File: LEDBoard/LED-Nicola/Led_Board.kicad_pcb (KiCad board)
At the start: 2 copper layers, 107.9 x 67.3 mm, 34 parts, among them J1 MOUNTING_HOLE, J10 CONN_01X02, J11 LED CONN 01X16, J12 CONN_01X02, J13 LED CONN 01X04, J2 MOUNTING_HOLE, J3 MOUNTING_HOLE, J4 MOUNTING_HOLE, J5 Arduino CONN 01X04, J6 Arduino CONN_01X04, J7 Arduino CONN_01X06, J8 VD 0 CONN_01X02, J9 CONN_01X02, Q1 MMBT, U1 SSR

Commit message: Changes
plz let me push
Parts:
- added BZ101: Buzzer, hyperCustom:nicolaBuzzer, F.Cu at (101.0, 81.9)
- added R101: R, Resistors_ThroughHole:R_Axial_DIN0309_L9.0mm_D3.2mm_P12.70mm_Horizontal, F.Cu at (178.4, 111.1)
- added R102: R, Resistors_ThroughHole:R_Axial_DIN0309_L9.0mm_D3.2mm_P12.70mm_Horizontal, F.Cu at (89.5, 95.9)
- Q1: value MMBT -> MMBT2222ALT1G
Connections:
- net /GND renamed GND
- U1 pad 5: /Buzzer -> Net-(R101-Pad2)
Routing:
- net /5V0: track 19.9 -> 72.9 mm, vias 0 -> 1
- net Net-(BZ101-Pad1): track 0.00 -> 15.1 mm
- net Net-(R101-Pad2): track 0.00 -> 12.1 mm
- added copper zone on B.Cu, net /GND

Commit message: new changes
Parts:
- removed BZ101: Buzzer, hyperCustom:nicolaBuzzer
- removed R101, R102: R, Resistors_ThroughHole:R_Axial_DIN0309_L9.0mm_D3.2mm_P12.70mm_Horizontal
- Q1: value MMBT2222ALT1G -> MMBT
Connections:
- D1 pad 1: GND -> /GND
- J1 pad 1: GND -> /GND
- J11 pad 10: GND -> /GND
- J11 pad 12: GND -> /GND
- J11 pad 14: GND -> /GND
- J11 pad 16: GND -> /GND
- J11 pad 2: GND -> /GND
- J11 pad 4: GND -> /GND
- J11 pad 6: GND -> /GND
- J11 pad 8: GND -> /GND
- J12 pad 2: GND -> /GND
- J13 pad 2: GND -> /GND
- J13 pad 4: GND -> /GND
- J2 pad 1: GND -> /GND
- J3 pad 1: GND -> /GND
- J4 pad 1: GND -> /GND
- J7 pad 2: GND -> /GND
- Q1 pad 2: GND -> /GND
- R11 pad 2: GND -> /GND
- R13 pad 2: GND -> /GND
- R9 pad 2: GND -> /GND
- U1 pad 5: Net-(R101-Pad2) -> /Buzzer
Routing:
- net /5V0: track 72.9 -> 19.9 mm, vias 1 -> 0
- net Net-(BZ101-Pad1): track 15.1 -> 0.00 mm
- net Net-(R101-Pad2): track 12.1 -> 0.00 mm
- net GND: track 2.06 -> 0.00 mm, vias 17 -> 0
- net /GND: track 0.00 -> 2.06 mm, vias 0 -> 17
- removed copper zone on B.Cu, net GND

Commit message: changes
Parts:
- removed G***: LOGO, hyperCustom:ParadigmLogo_1x1
- added BZ101: , hyperCustom:nicolaBuzzer, F.Cu at (101.0, 81.9)
- added R101: , Resistors_ThroughHole:R_Axial_DIN0309_L9.0mm_D3.2mm_P12.70mm_Horizontal, F.Cu at (178.4, 111.1)
- added R102: , Resistors_ThroughHole:R_Axial_DIN0309_L9.0mm_D3.2mm_P12.70mm_Horizontal, F.Cu at (89.5, 95.9)
- D1: value LED -> (none)
- J1, J2, J3, J4: value MOUNTING_HOLE -> (none)
- J10, J12, J9: value CONN_01X02 -> (none)
- J11: value LED CONN 01X16 -> (none)
- J13: value LED CONN 01X04 -> (none)
- J5: value Arduino CONN 01X04 -> (none)
- J6: value Arduino CONN_01X04 -> (none)
- J7: value Arduino CONN_01X06 -> (none)
- J8: value VD 0 CONN_01X02 -> (none)
- R1, R15, R16, R17, R2, R3, R4, R5, R6, R7: value 220 -> (none)
- R10, R11, R12, R13, R14, R8, R9: value R -> (none)
- moved D1 19.4 mm to (166.4, 80.0), turned to 270 degrees
- moved R13 12.5 mm to (175.3, 88.9), turned to 270 degrees
- moved R14 11.7 mm to (170.2, 80.0), turned to 270 degrees
- moved R12 9.25 mm to (179.1, 88.9)
- moved J8 9.00 mm to (193.0, 83.8)
- moved R8 8.98 mm to (177.8, 80.0)
- moved J10 8.78 mm to (193.0, 92.7)
- moved R9 7.41 mm to (174.0, 80.0), turned to 270 degrees
- moved R11 5.24 mm to (175.3, 69.8), turned to 270 degrees
- moved R10 4.02 mm to (180.3, 69.8)
- moved U1 1.27 mm to (167.6, 101.6), turned to 90 degrees
- moved J9 0.11 mm to (193.0, 74.9)
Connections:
- J5 pad 1: /A1 -> /A0
- J5 pad 2: /A0 -> /24V
- J5 pad 3: /24V -> /5V0
- J5 pad 4: /5V0 -> /Transistor
- J6 pad 1: /A5 -> /A4
- J6 pad 2: /A4 -> /A3
- J6 pad 3: /A3 -> /A2
- J6 pad 4: /A2 -> /A1
- J7 pad 1: (no net) -> /ArduinoLED
- J7 pad 2: /GND -> /5V
- J7 pad 3: /A9 -> /A8
- J7 pad 4: /A8 -> /A7
- J7 pad 5: /A7 -> /A6
- J7 pad 6: /A6 -> /A5
- Q1 pad 1: /A7 -> /Transistor
- R17 pad 2: /A9 -> /ArduinoLED
- U1 pad 5: /Buzzer -> Net-(R101-Pad2)
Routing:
- net /ArduinoLED: track 0.00 -> 46.5 mm
- net /A7: track 93.4 -> 49.0 mm, vias 1 -> 0
- net /A9: track 43.6 -> 0.00 mm
- net /24V: track 58.5 -> 39.3 mm, vias 2 -> 0
- net /VDO0: track 31.7 -> 14.9 mm
- net Net-(BZ101-Pad1): track 0.00 -> 15.1 mm
- net Net-(R101-Pad2): track 0.00 -> 15.0 mm, vias 0 -> 1
- net Net-(D1-Pad2): track 15.6 -> 4.02 mm
- net /5V: track 0.00 -> 11.0 mm, vias 0 -> 1
- net /Transistor: track 0.00 -> 6.69 mm
- net Net-(Q1-Pad3): track 7.87 -> 12.8 mm
- net /VDI1: track 8.73 -> 4.96 mm
- net /VDO2: track 13.1 -> 9.84 mm
- net /A0: track 58.8 -> 61.7 mm, vias 2 -> 0
- net /VDO1: track 13.1 -> 10.2 mm
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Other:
- board text added: "PWR IN"
- board text added: "PWR OUT"
- board text removed: "Nicola Duffy July 2017"
- board text removed: "PWR"

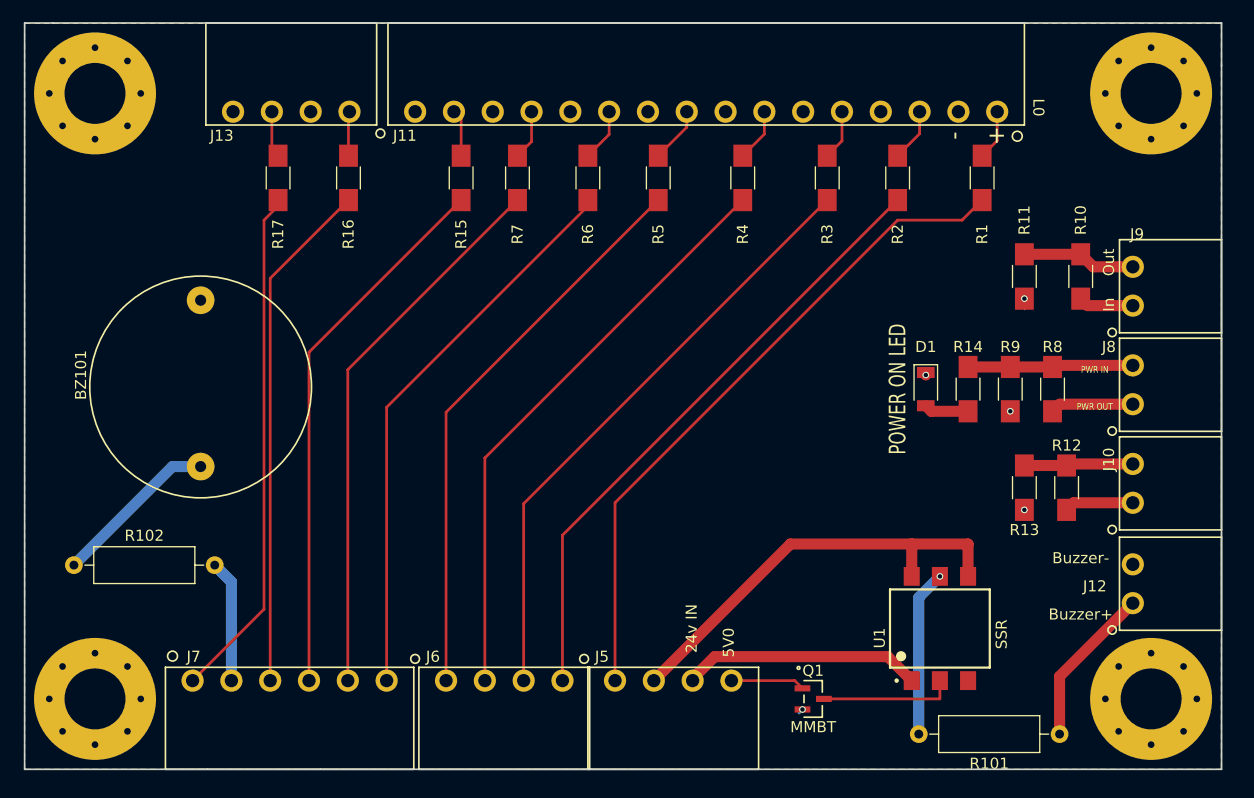
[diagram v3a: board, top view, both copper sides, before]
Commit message: Finalized LED Board
Added Silkscreen for all sides of the board and all connectors. Moved
the Placement of the Power on LED to show then the arduino is
outputting power correctly. Slightly move components to make it more
efficient.
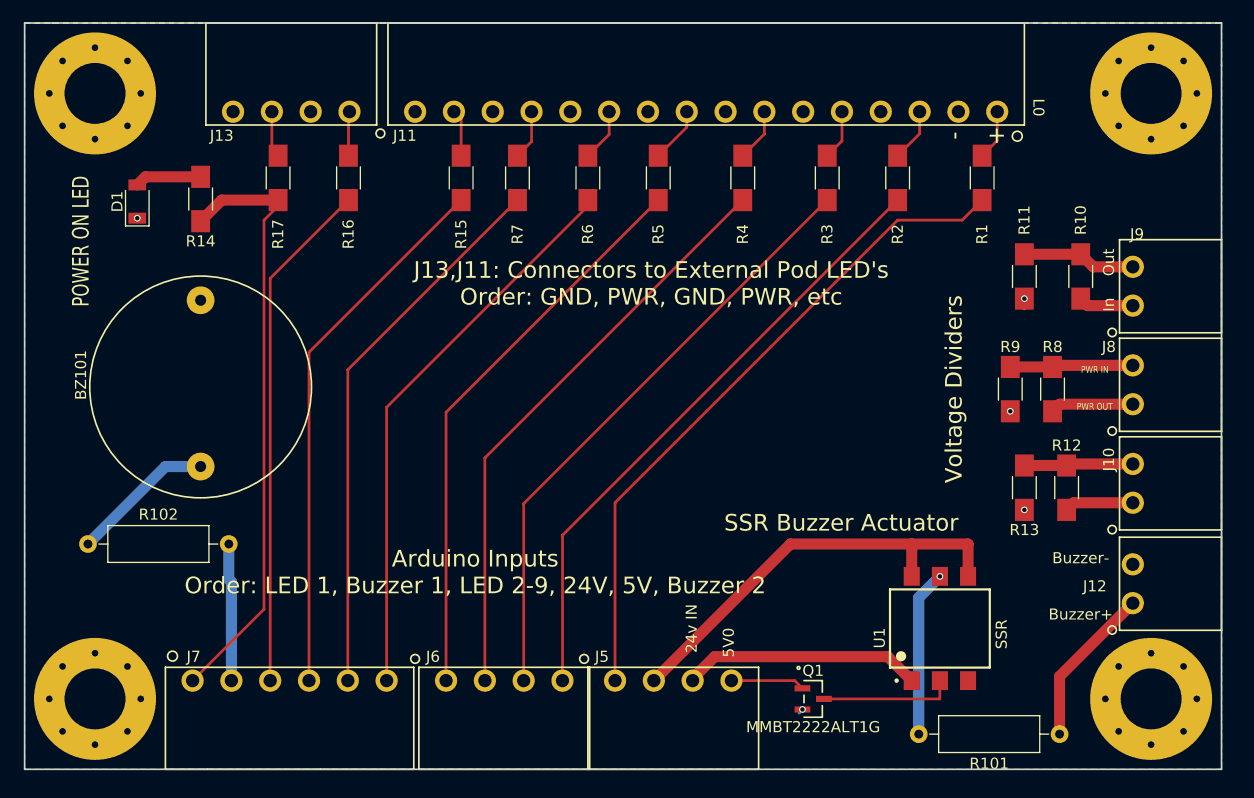
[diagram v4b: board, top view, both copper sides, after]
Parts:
- BZ101: value (none) -> Buzzer
- D1: value (none) -> LED
- J1, J2, J3, J4: value (none) -> MOUNTING_HOLE
- J10, J12, J9: value (none) -> CONN_01X02
- J11: value (none) -> LED CONN 01X16
- J13: value (none) -> LED CONN 01X04
- J5: value (none) -> Arduino CONN 01X04
- J6: value (none) -> Arduino CONN_01X04
- J7: value (none) -> Arduino CONN_01X06
- J8: value (none) -> VD 0 CONN_01X02
- Q1: value MMBT -> MMBT2222ALT1G
- R1, R15, R16, R17, R2, R3, R4, R5, R6, R7: value (none) -> 220
- R10, R101, R102, R11, R12, R13, R14, R8, R9: value (none) -> R
- moved D1 73.1 mm to (95.2, 63.1), turned to 90 degrees
- moved R14 71.3 mm to (101.0, 62.9), turned to 90 degrees
- moved R102 2.29 mm to (90.8, 94.0)
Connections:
- R14 pad 1: /VDO0 -> /ArduinoLED
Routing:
- net /ArduinoLED: track 46.5 -> 54.3 mm
- net /VDO0: track 14.9 -> 11.1 mm
- net Net-(BZ101-Pad1): track 15.1 -> 13.1 mm
- net Net-(D1-Pad2): track 4.02 -> 6.02 mm
- net /5V: track 11.0 -> 12.4 mm
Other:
- board text added: "Arduino Inputs Order: LED 1, Buzzer 1, LED 2-9, 24V, 5V, Buzzer 2"
- board text added: "J13,J11: Connectors to External Pod LED's Order: GND, PWR, GND, PWR, etc"
- board text added: "SSR Buzzer Actuator"
- board text added: "Voltage Dividers"

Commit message: Made a couple final changes to the LED Board- Should be good to go
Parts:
- added J101: CONN_01X01, hyperCustom:CONN_PHOENIX_1844210_1PIN, F.Cu at (152.7, 114.3)
- Q1: value MMBT2222ALT1G -> MMBT
- moved Q1 5.45 mm to (161.5, 109.3)
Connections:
- net /GND renamed GND
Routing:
- net /Transistor: track 6.69 -> 13.4 mm
- net Net-(Q1-Pad3): track 12.8 -> 7.69 mm
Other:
- board text added: "Arduino Inputs Order: LED 1, Buzzer 1, LED 2-9, 24V, 5V, Buzzer 2, GND"
- board text removed: "Arduino Inputs Order: LED 1, Buzzer 1, LED 2-9, 24V, 5V, Buzzer 2"

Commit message: Added Connector
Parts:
- removed J101: CONN_01X01, hyperCustom:CONN_PHOENIX_1844210_1PIN
- J5: value Arduino CONN 01X04 -> CONN_01X06; footprint hyperCustom:CONN_PHOENIX_1844236_4PIN -> hyperCustom:CONN_PHOENIX_1844252_6PIN
- Q1: value MMBT -> MMBT2222ALT1G
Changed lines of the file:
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@@
   (general
     (links 61)
-    (no_connects 21)
+    (no_connects 0)
     (area 85.014999 46.914999 193.115001 114.375001)
     (thickness 1.6)
@@
     (tracks 114)
     (zones 0)
-    (modules 37)
+    (modules 36)
     (nets 37)
   )
@@
       (effects (font (size 1 1) (thickness 0.15)))
     )
-    (fp_text value MMBT (at 2.54 0 360) (layer F.SilkS)
+    (fp_text value MMBT2222ALT1G (at 2.54 0 360) (layer F.SilkS)
       (effects (font (size 1 1) (thickness 0.15)))
     )
@@
   )
   (module hyperCustom:CONN_PHOENIX_1844236_4PIN (layer F.Cu)
-    (at 135.89 114.3)
-    (fp_text reference J5 (at 1.27 -10.16) (layer F.SilkS)
-      (effects (font (size 1 1) (thickness 0.15)))
-    )
-    (fp_text value "Arduino CONN 01X04" (at 11.43 2.54) (layer F.Fab)
-      (effects (font (size 1 1) (thickness 0.15)))
-    )
-    (fp_circle (center -0.34 -9.96) (end 0.05 -9.9) (layer F.SilkS) (width 0.15))
-    (fp_line (start 0 -9.2) (end 15.4 -9.2) (layer F.SilkS) (width 0.15))
-    (fp_line (start 15.4 0) (end 15.4 -9.2) (layer F.SilkS) (width 0.15))
-    (fp_line (start 0 0) (end 0 -9.2) (layer F.SilkS) (width 0.15))
-    (fp_line (start 0 0) (end 15.4 0) (layer F.SilkS) (width 0.15))
-    (pad 1 thru_hole circle (at 2.45 -8) (size 2 2) (drill 1.2) (layers *.Cu *.Mask)
-      (net 8 /A0))
-    (pad 2 thru_hole circle (at 5.95 -8) (size 2 2) (drill 1.2) (layers *.Cu *.Mask)
-      (net 9 /24V))
-    (pad 3 thru_hole circle (at 9.45 -8) (size 2 2) (drill 1.2) (layers *.Cu *.Mask)
-      (net 30 /5V0))
-    (pad 4 thru_hole circle (at 12.95 -8) (size 2 2) (drill 1.2) (layers *.Cu *.Mask)
-      (net 33 /Transistor))
-  )
-  (module hyperCustom:CONN_PHOENIX_1844236_4PIN (layer F.Cu)
     (at 120.65 114.3)
     (fp_text reference J6 (at 1.27 -10.16) (layer F.SilkS)
@@
     )
   )
-  (module hyperCustom:CONN_PHOENIX_1844210_1PIN (layer F.Cu)
-    (at 152.654 114.3)
-    (fp_text reference J101 (at 4.67 -10.5) (layer F.SilkS)
-      (effects (font (size 1 1) (thickness 0.15)))
-    )
-    (fp_text value CONN_01X01 (at 0.05 4.17) (layer F.Fab)
-      (effects (font (size 1 1) (thickness 0.15)))
-    )
-    (fp_circle (center 0.03 -9.86) (end 0.4 -9.79) (layer F.SilkS) (width 0.15))
-    (fp_line (start 0 -9.2) (end 4.6 -9.2) (layer F.SilkS) (width 0.15))
-    (fp_line (start 4.6 0) (end 4.6 -9.2) (layer F.SilkS) (width 0.15))
+  (module hyperCustom:CONN_PHOENIX_1844252_6PIN (layer F.Cu)
+    (at 135.89 114.3)
+    (fp_text reference J5 (at 23.418 -7.012 90) (layer F.SilkS)
+      (effects (font (size 1 1) (thickness 0.15)))
+    )
+    (fp_text value CONN_01X06 (at 11.61 2.57) (layer F.Fab)
+      (effects (font (size 1 1) (thickness 0.15)))
+    )
+    (fp_circle (center 0.64 -10.21) (end 0.94 -9.88) (layer F.SilkS) (width 0.15))
+    (fp_line (start 22.4 0) (end 22.4 -9.2) (layer F.SilkS) (width 0.15))
+    (fp_line (start 0 -9.2) (end 22.4 -9.2) (layer F.SilkS) (width 0.15))
     (fp_line (start 0 0) (end 0 -9.2) (layer F.SilkS) (width 0.15))
-    (fp_line (start 0 0) (end 4.6 0) (layer F.SilkS) (width 0.15))
+    (fp_line (start 0 0) (end 22.4 0) (layer F.SilkS) (width 0.15))
     (pad 1 thru_hole circle (at 2.45 -8) (size 2 2) (drill 1.2) (layers *.Cu *.Mask)
-      (net 36 GND))
+      (net 8 /A0))
+    (pad 2 thru_hole circle (at 5.95 -8) (size 2 2) (drill 1.2) (layers *.Cu *.Mask)
+      (net 9 /24V))
+    (pad 3 thru_hole circle (at 9.45 -8) (size 2 2) (drill 1.2) (layers *.Cu *.Mask)
+      (net 30 /5V0))
+    (pad 4 thru_hole circle (at 12.95 -8) (size 2 2) (drill 1.2) (layers *.Cu *.Mask)
+      (net 33 /Transistor))
+    (pad 5 thru_hole circle (at 16.45 -8) (size 2 2) (drill 1.2) (layers *.Cu *.Mask)
+      (net 36 GND))
+    (pad 6 thru_hole circle (at 19.95 -8) (size 2 2) (drill 1.2) (layers *.Cu *.Mask))
   )
   (gr_text "Arduino Inputs\nOrder: LED 1, Buzzer 1, LED 2-9, 24V, 5V, Buzzer 2, GND" (at 125.73 96.52) (layer F.SilkS)

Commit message: Final Changes
Good to go. Added the correct 5 pin connector.
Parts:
- removed J5: CONN_01X06, hyperCustom:CONN_PHOENIX_1844252_6PIN
- added J101: CONN_01X05, hyperCustom:CONN_PHOENIX_1844252_5PIN, F.Cu at (136.5, 114.3)
- Q1: value MMBT2222ALT1G -> MMBT
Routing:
- net /24V: track 39.3 -> 42.0 mm
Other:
- board text added: "Nicola Duffy Paradigm 2017"

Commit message: Added logo
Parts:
- added ?: , hyperCustom:ParadigmLogo_0_5x0_5, F.Cu at (157.5, 81.3)
